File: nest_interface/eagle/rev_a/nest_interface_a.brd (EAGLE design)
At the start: 133.3 x 110.5 mm, 111 parts, among them J1 MOLEX_MICRO_USB_B_047346, J10 CONN_BLOCK_2, J11 CONN_BLOCK_2, J12 CONN_BLOCK_2, J13 CONN_BLOCK_2, J14 CONN_BLOCK_3, J15 CONN_BLOCK_3, J16 CONN_BLOCK_7, J17 CONN_BLOCK_7, J18 CONN_BLOCK_8, J19 CONN_BLOCK_8, J2 MOLEX_MICRO_USB_B_047346, J20 CONN_BLOCK_8, J21 CONN_BLOCK_8, J5 PJ-036A-SMT, J6 CONN_BLOCK_2, J7 CONN_BLOCK_2, J8 CONN_BLOCK_2, J9 CONN_BLOCK_2, U1 EPIC-CORE_A, U2 MSP430F1611IPM, U3 FT232RL, U4 FT232RL, U5 MPC1825, U6 TC1262, U7 PCA9575, U8 PCA9575, Y1 FC-135_32.768KA-A3

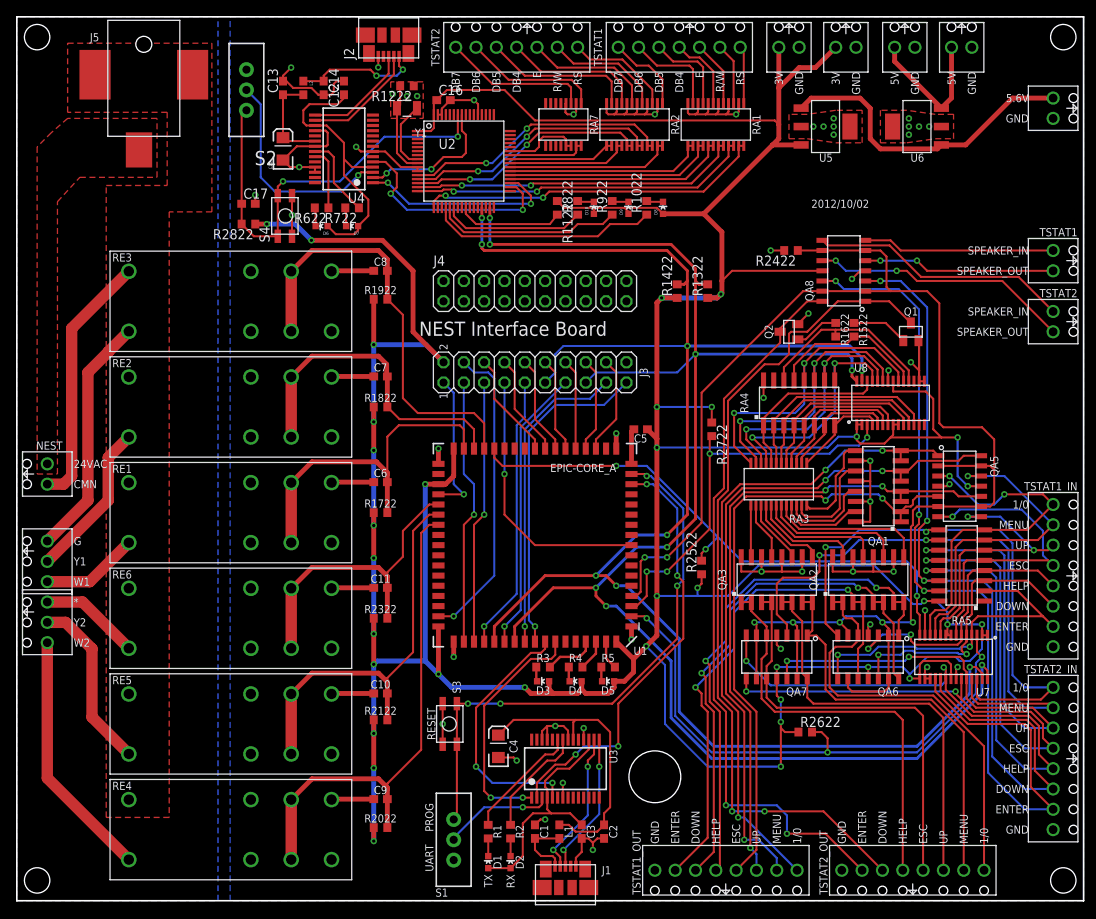
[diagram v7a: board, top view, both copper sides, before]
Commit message: labels cleaned up, looks good
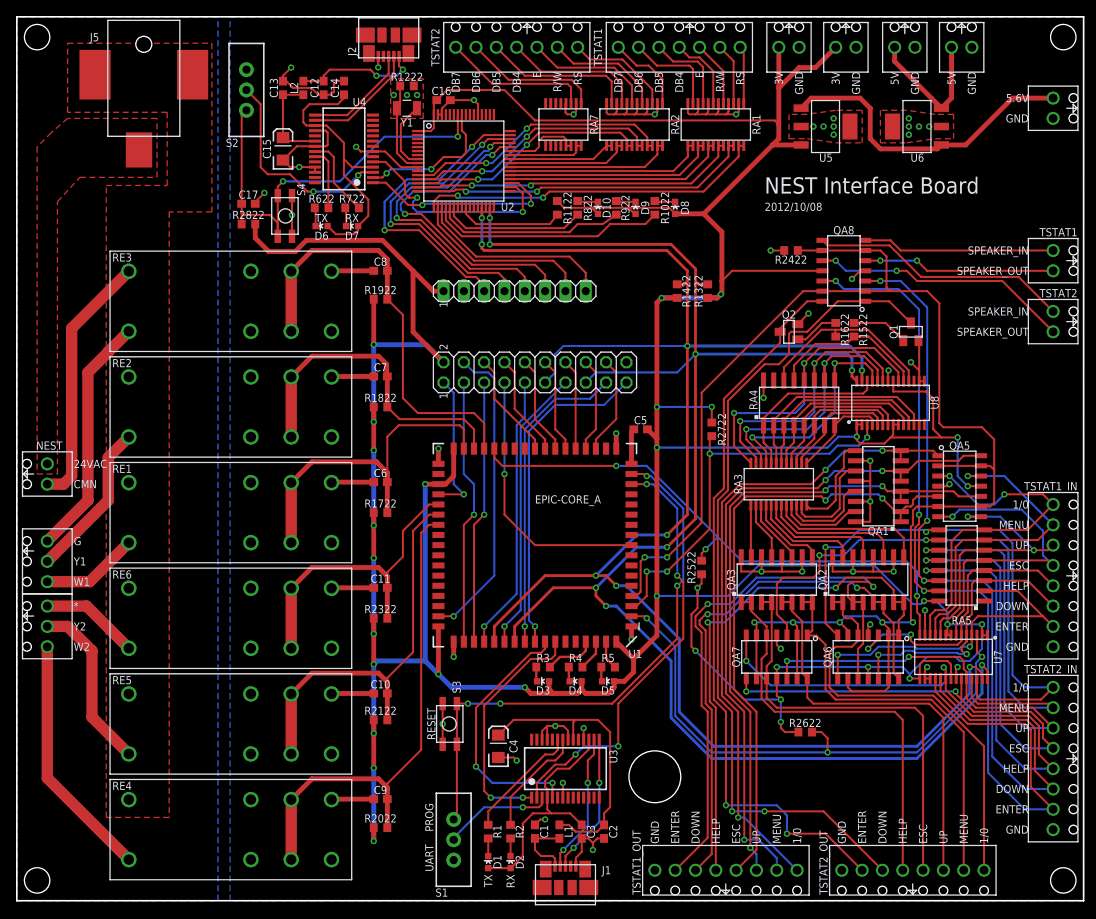
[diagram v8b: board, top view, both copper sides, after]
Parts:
- removed J4: (no value), pinhead:2X10
- added JP1: (no value), pinhead:1X08
- moved D8 1.52 mm to (82.3, 86.6)
- moved R1022 1.02 mm to (79.8, 86.6)
- moved D9 0.89 mm to (77.3, 86.6)
- moved D10 0.51 mm to (72.6, 86.6)
- moved R922 0.51 mm to (74.9, 86.6)
- moved J15 0.51 mm to (3.81, 34.3)
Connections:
- removed net P1.6: U2.18
- removed net P1.7: U2.19
- removed net P5.0: U2.44
- removed net P5.1: U2.45
- removed net P5.2: U2.46
- removed net P5.3: U2.47
- new net LCDP_MISO1: JP1.4, U2.46
- new net LCDP_MOSI1: JP1.5, U2.45
- new net LCDP_P1.6: JP1.7, U2.18
- new net LCDP_P1.7: JP1.8, U2.19
- new net LCDP_STE1: JP1.6, U2.44
- new net LCDP_UCLK1: JP1.3, U2.47
- net GND: now also JP1.2
- net VCC: now also JP1.1
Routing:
- net LCDP_STE1: track 0.00 -> 40.8 mm, vias 0 -> 2
- net LCDP_MOSI1: track 0.00 -> 40.2 mm, vias 0 -> 2
- net LCDP_MISO1: track 0.00 -> 39.6 mm, vias 0 -> 2
- net LCDP_UCLK1: track 0.00 -> 38.8 mm, vias 0 -> 2
- net LCDP_P1.7: track 0.00 -> 24.8 mm
- net LCDP_P1.6: track 0.00 -> 22.9 mm
- net TSTAT1_ENTER_OUT: track 64.8 -> 75.8 mm
- net VCC: track 605.9 -> 602.7 mm, vias 35 -> 32
- net RST1: track 53.7 -> 55.2 mm
- net TSTAT1_DOWN_OUT: track 67.9 -> 69.4 mm
- net N$53: track 2.07 -> 3.24 mm
- net N$8: track 28.7 -> 29.7 mm
- net RST_USB1: track 27.4 -> 26.7 mm, vias 1 -> 2
- net GND: track 224.1 -> 224.8 mm
- net N$3: track 18.3 -> 17.6 mm
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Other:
- board text added: "2012/10/08"
- board text removed: "2012/10/02"
